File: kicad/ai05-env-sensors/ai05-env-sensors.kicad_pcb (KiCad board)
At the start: 4 copper layers, 23 x 20 mm, 1 part, among them CN1 Leafony Bus

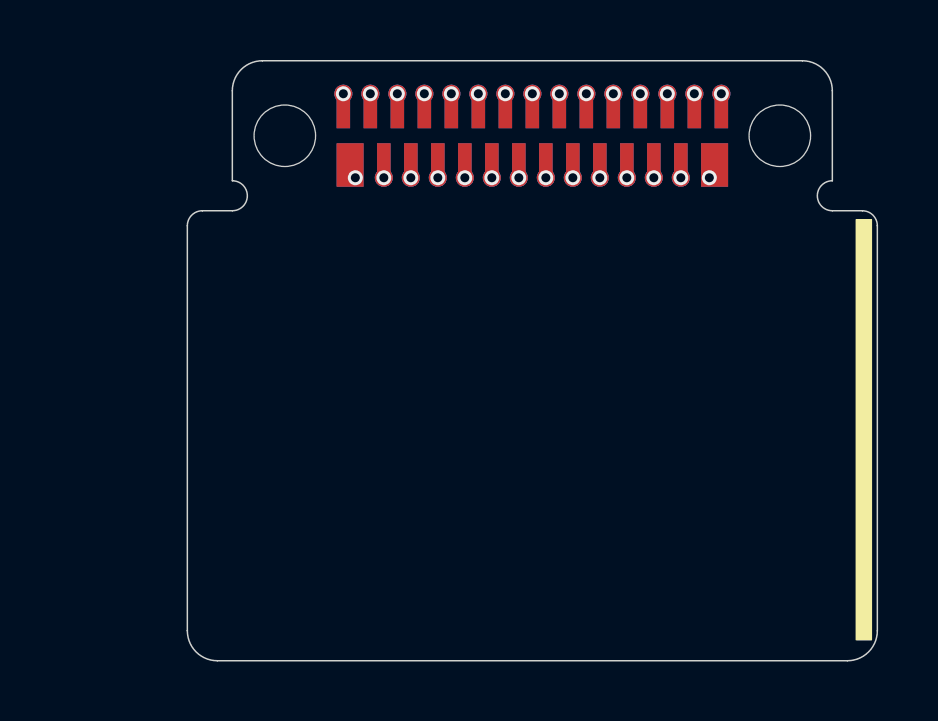
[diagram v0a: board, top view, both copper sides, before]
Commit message: Add new footprints for various sensors and connectors
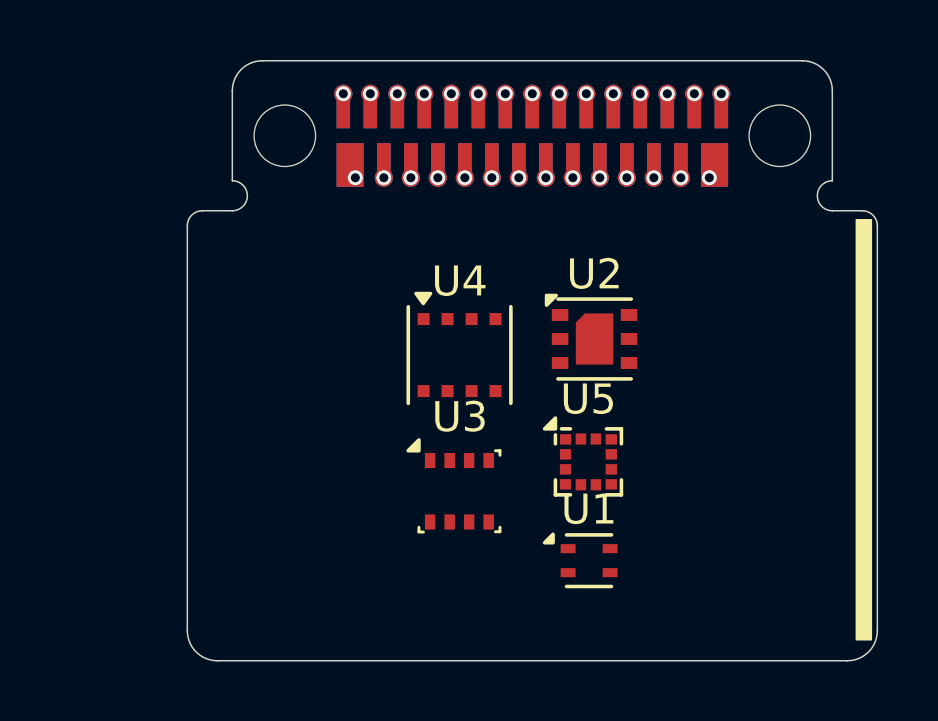
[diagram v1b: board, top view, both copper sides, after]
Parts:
- added U1: SHT40-AD1B-R2, AI05:Sensirion_DFN-4_1.5x1.5mm_P0.8mm_SHT4x_NoCentralPad, F.Cu at (36.9, 41.7)
- added U2: SGP40-D-R4, AI05:Sensirion_DFN-6-1EP_2.44x2.44mm_P0.8mm_SGP40, F.Cu at (37.1, 34.3)
- added U3: BME280, AI05:Bosch_LGA-8_2.5x2.5mm_P0.65mm_ClockwisePinNumbering, F.Cu at (32.6, 39.4)
- added U4: BME680, AI05:Bosch_LGA-8_3x3mm_P0.8mm_ClockwisePinNumbering_Recommended, F.Cu at (32.6, 34.8)
- added U5: LIS2DW12TR, AI05:LGA-12_2x2mm_P0.5mm, F.Cu at (36.9, 38.4)

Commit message: レイアウト完成
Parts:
- added C2: 1u(M)/10V/X5R, Capacitor_SMD:C_0402_1005Metric, F.Cu at (32.4, 35.5)
- added C20: 0.1u(K)/50V/X7R, Capacitor_SMD:C_0402_1005Metric, F.Cu at (33.8, 41.1)
- added C21: 0.1u(K)/50V/X7R, Capacitor_SMD:C_0402_1005Metric, F.Cu at (42.3, 43.1)
- added C22: 0.1u(K)/50V/X7R, Capacitor_SMD:C_0402_1005Metric, F.Cu at (45.0, 41.0)
- added C23: 0.1u(K)/50V/X7R, Capacitor_SMD:C_0402_1005Metric, F.Cu at (37.2, 43.3)
- added C24: 0.1u(K)/50V/X7R, Capacitor_SMD:C_0402_1005Metric, F.Cu at (40.4, 41.0)
- added C25: 0.1u(K)/50V/X7R, Capacitor_SMD:C_0402_1005Metric, F.Cu at (37.0, 35.0)
- added C26: 0.1u(K)/50V/X7R, Capacitor_SMD:C_0402_1005Metric, F.Cu at (36.4, 32.8)
- added C27: 10u(M)/35V/X5R, Capacitor_SMD:C_0603_1608Metric, F.Cu at (38.4, 35.0)
- added C3: 1u(M)/10V/X5R, Capacitor_SMD:C_0402_1005Metric, F.Cu at (27.8, 34.6)
- added J1: Conn_01x04_Pin, AI05:PinHeader_1x04_P2.54mm_Horizontal, F.Cu at (24.8, 41.2)
- added R10: 4.7Ω(J), Resistor_SMD:R_0402_1005Metric, F.Cu at (28.9, 32.2)
- added R18: 2.7kΩ(J), Resistor_SMD:R_0402_1005Metric, F.Cu at (41.5, 31.8)
- added R19: 2.7kΩ(J), Resistor_SMD:R_0402_1005Metric, F.Cu at (41.5, 32.9)
- moved U3 10.6 mm to (43.0, 41.0)
- moved U4 8.23 mm to (38.0, 41.0)
- moved U2 7.06 mm to (30.1, 35.0)
- moved U1 4.94 mm to (32.0, 41.0)
- moved U5 3.85 mm to (35.0, 35.0)
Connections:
- U1 pad 1: unconnected-(U1-SDA-Pad1) -> /SDA
- U1 pad 2: unconnected-(U1-SCL-Pad2) -> /SCL
- U1 pad 3: unconnected-(U1-VDD-Pad3) -> +3V3
- U1 pad 4: unconnected-(U1-VSS-Pad4) -> GND
- U2 pad 1: unconnected-(U2-VDD-Pad1) -> Net-(U2-VDD)
- U2 pad 2: unconnected-(U2-VSS-Pad2) -> GND
- U2 pad 3: unconnected-(U2-SDA-Pad3) -> /SDA
- U2 pad 4: unconnected-(U2-n/a-Pad4) -> GND
- U2 pad 5: unconnected-(U2-VDDH-Pad5) -> +3V3
- U2 pad 6: unconnected-(U2-SCL-Pad6) -> /SCL
- U2 pad 7: unconnected-(U2-EP-Pad7) -> GND
- U3 pad 1: unconnected-(U3-GND-Pad1) -> GND
- U3 pad 2: unconnected-(U3-CSB-Pad2) -> +3V3
- U3 pad 3: unconnected-(U3-SDI-Pad3) -> /SDA
- U3 pad 4: unconnected-(U3-SCK-Pad4) -> /SCL
- U3 pad 5: unconnected-(U3-SDO-Pad5) -> GND
- U3 pad 6: unconnected-(U3-VDDIO-Pad6) -> +3V3
- U3 pad 7: unconnected-(U3-GND-Pad7) -> GND
- U3 pad 8: unconnected-(U3-VDD-Pad8) -> +3V3
- U4 pad 1: unconnected-(U4-GND-Pad1) -> GND
- U4 pad 2: unconnected-(U4-CSB-Pad2) -> +3V3
- U4 pad 3: unconnected-(U4-SDI-Pad3) -> /SDA
- U4 pad 4: unconnected-(U4-SCK-Pad4) -> /SCL
- U4 pad 5: unconnected-(U4-SDO-Pad5) -> GND
- U4 pad 6: unconnected-(U4-VDDIO-Pad6) -> +3V3
- U4 pad 7: unconnected-(U4-GND-Pad7) -> GND
- U4 pad 8: unconnected-(U4-VDD-Pad8) -> +3V3
- U5 pad 1: unconnected-(U5-SCL/SPC-Pad1) -> /SCL
- U5 pad 10: unconnected-(U5-VDD_IO-Pad10) -> +3V3
- U5 pad 12: unconnected-(U5-INT1-Pad12) -> /D3
- U5 pad 2: unconnected-(U5-~{CS}-Pad2) -> +3V3
- U5 pad 3: unconnected-(U5-SDO/SA0-Pad3) -> GND
- U5 pad 4: unconnected-(U5-SDA/SDI/SDO-Pad4) -> /SDA
- U5 pad 6: unconnected-(U5-GND-Pad6) -> GND
- U5 pad 7: unconnected-(U5-RES-Pad7) -> GND
- U5 pad 8: unconnected-(U5-GND-Pad8) -> GND
- U5 pad 9: unconnected-(U5-VDD-Pad9) -> +3V3
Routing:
- net /SCL: track 0.00 -> 49.6 mm, vias 1 -> 7
- net /SDA: track 0.00 -> 40.1 mm, vias 1 -> 7
- net +3V3: track 0.00 -> 25.3 mm, vias 1 -> 15
- net GND: track 0.00 -> 23.5 mm, vias 1 -> 26
- net /D3: track 0.00 -> 11.1 mm, vias 1 -> 2
- net Net-(U2-VDD): track 0.00 -> 2.68 mm
- added copper zone on In2.Cu, net +3V3
- added copper zone on B.Cu, net GND
- added copper zone on F.Cu, net GND
- added copper zone on In1.Cu, net GND
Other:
- board text added: "GND"
- board text added: "SCL"
- board text added: "SDA"
- board text added: "V33"

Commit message: 面付・ガーバー出力
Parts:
- moved J1 0.06 mm to (24.9, 41.2)
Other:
- board text added: "Leafony AI05 Env Sensors"
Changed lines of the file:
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@@
 	(footprint "AI05:PinHeader_1x04_P2.54mm_Horizontal"
 		(layer "F.Cu")
-		(at 24.7905 41.205 180)
+		(at 24.85 41.205 180)
 		(descr "Through hole angled pin header, 1x04, 2.54mm pitch, 6mm pin length, single row")
 		(tags "Through hole angled pin header THT 1x04 2.54mm single row")
@@
 			(at 4.385 -2.27 0)
 			(layer "F.SilkS")
+			(hide yes)
 			(effects
 				(font
@@
 		(layer "Edge.Cuts")
 	)
+	(gr_text "Leafony\nAI05\nEnv Sensors"
+		(at 35.45 37.6 0)
+		(layer "B.SilkS")
+		(effects
+			(font
+				(size 1 1)
+				(thickness 0.15)
+			)
+			(justify mirror)
+		)
+	)
 	(gr_text "SCL"
 		(at 27 33.7 0)
@@
 	)
 	(zone
-		(net "/SCL")
+		(net "/SDA")
 		(layer "In1.Cu")
 		(hatch none 0.1)
-		(priority 30001)
+		(priority 30000)
 		(attr
 			(teardrop
@@
 		(polygon
 			(pts
-				(xy 39.599844 29.108735) (xy 39.741265 29.250156) (xy 39.952291 29.145196) (xy 39.954104 28.895896)
-				(xy 39.704804 28.897708)
+				(xy 38.95 29.295196) (xy 39.15 29.295196) (xy 39.225 29.07176) (xy 39.05 28.894196) (xy 38.875 29.07176)
 			)
 		)
@@
 	)
 	(zone
-		(net "/SDA")
+		(net "/SCL")
 		(layer "In1.Cu")
 		(hatch none 0.1)
-		(priority 30000)
+		(priority 30001)
 		(attr
 			(teardrop
@@
 		(polygon
 			(pts
-				(xy 38.95 29.295196) (xy 39.15 29.295196) (xy 39.225 29.07176) (xy 39.05 28.894196) (xy 38.875 29.07176)
+				(xy 39.599844 29.108735) (xy 39.741265 29.250156) (xy 39.952291 29.145196) (xy 39.954104 28.895896)
+				(xy 39.704804 28.897708)
 			)
 		)
